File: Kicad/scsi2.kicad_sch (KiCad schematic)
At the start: 29 parts, among them J3 TO-LED, J4 TO-MB, J8 TO-A3000-LED, J9 TO-A3000-MB, U4 NCR53c710 SCSI Host Controller, U7 SST39SF010, Y1 Abracon ACO-50MHz

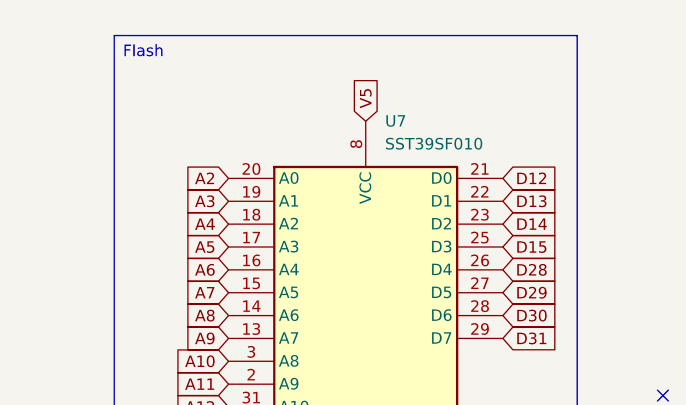
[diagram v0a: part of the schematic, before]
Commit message: Rename all Uxx parts from U1 to U13 for consistency
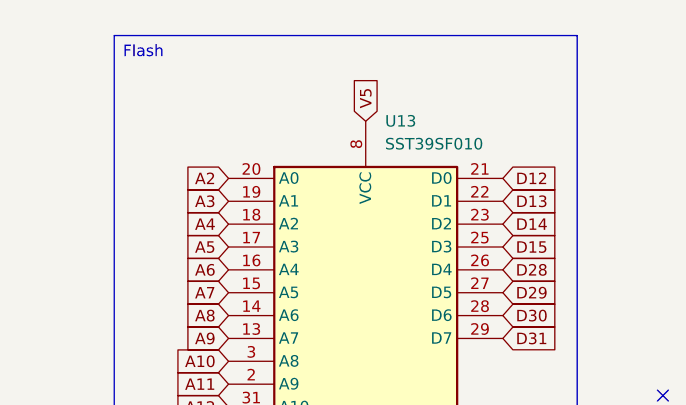
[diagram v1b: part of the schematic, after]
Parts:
- renumbered U4 to U10, U7 to U13
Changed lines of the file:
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@@
 		(dnp no)
 		(fields_autoplaced yes)
-		(property "Reference" "U7"
+		(property "Reference" "U13"
 			(at 259.9533 24.13 0)
 			(effects
@@
 			(project ""
 				(path "/8f9f4021-47aa-41d9-bea7-f6ccf72098bb/2daf4fe3-1e72-4ad5-914a-264df02f69b3"
-					(reference "U7")
+					(reference "U13")
 					(unit 1)
 				)
@@
 		(dnp no)
 		(fields_autoplaced yes)
-		(property "Reference" "U4"
+		(property "Reference" "U10"
 			(at 107.188 12.446 0)
 			(effects
@@
 			(project ""
 				(path "/8f9f4021-47aa-41d9-bea7-f6ccf72098bb/2daf4fe3-1e72-4ad5-914a-264df02f69b3"
-					(reference "U4")
+					(reference "U10")
 					(unit 2)
 				)
@@
 		(dnp no)
 		(fields_autoplaced yes)
-		(property "Reference" "U4"
+		(property "Reference" "U10"
 			(at 32.258 14.986 0)
 			(effects
@@
 			(project ""
 				(path "/8f9f4021-47aa-41d9-bea7-f6ccf72098bb/2daf4fe3-1e72-4ad5-914a-264df02f69b3"
-					(reference "U4")
+					(reference "U10")
 					(unit 1)
 				)

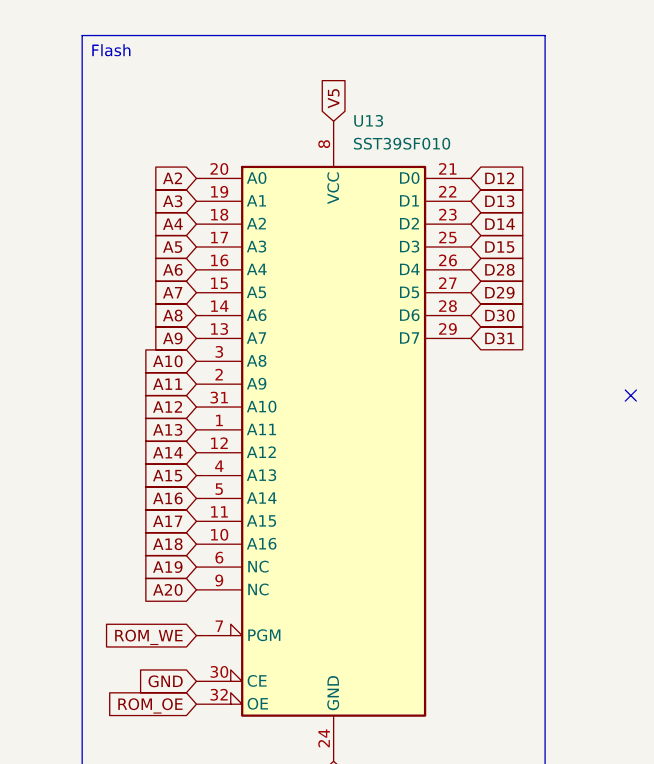
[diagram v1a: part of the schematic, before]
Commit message: Update Flash part symbol
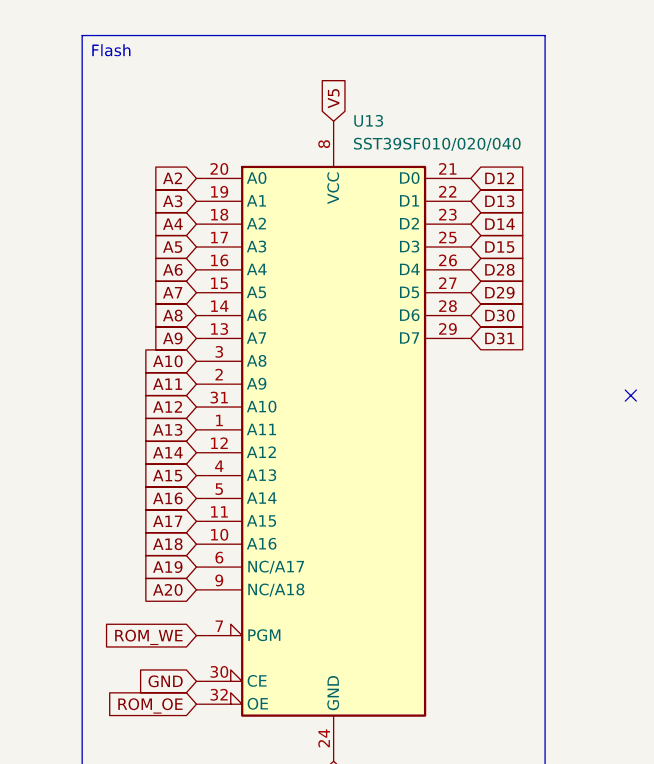
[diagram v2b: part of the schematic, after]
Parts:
- U13: value SST39SF010 -> SST39SF010/020/040
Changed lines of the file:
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@@
 			)
 		)
-		(property "Value" "SST39SF010"
+		(property "Value" "SST39SF010/020/040"
 			(at 259.9533 26.67 0)
 			(effects
@@
 			)
 		)
-		(property "Datasheet" "http://ww1.microchip.com/downloads/en/DeviceDoc/25022B.pdf"
+		(property "Datasheet" "https://ww1.microchip.com/downloads/aemDocuments/documents/MPD/ProductDocuments/DataSheets/SST39SF010A-SST39SF020A-SST39SF040-Data-Sheet-DS20005022.pdf"
 			(at 257.81 53.34 0)
 			(effects

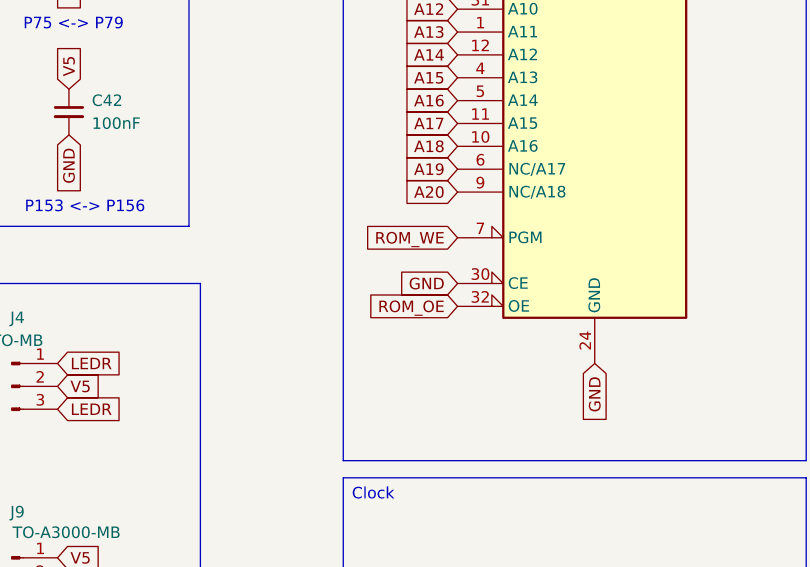
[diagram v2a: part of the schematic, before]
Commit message: ROM_WE Single net Issue #3
Connect ROM_WE to CPLD. Also connect ROM_CE.
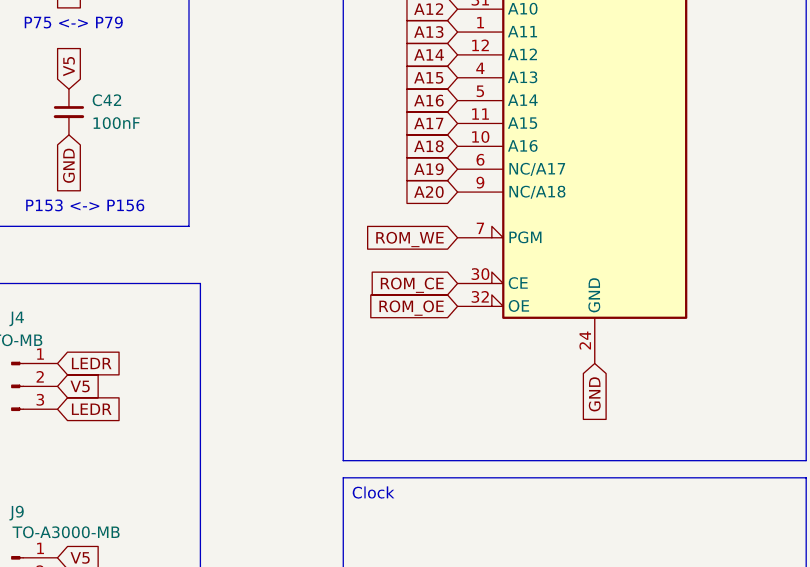
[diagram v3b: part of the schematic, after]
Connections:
- net GND: no longer U13.30 (CE)
- new net ROM_CE: U13.30 (CE)
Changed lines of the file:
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@@
 		)
 	)
-	(global_label "GND"
+	(global_label "ROM_CE"
 		(shape input)
 		(at 242.57 86.36 180)
@@
 		)
 		(property "Intersheetrefs" "${INTERSHEET_REFS}"
-			(at 235.7143 86.36 0)
+			(at 232.1463 86.36 0)
 			(effects
 				(font

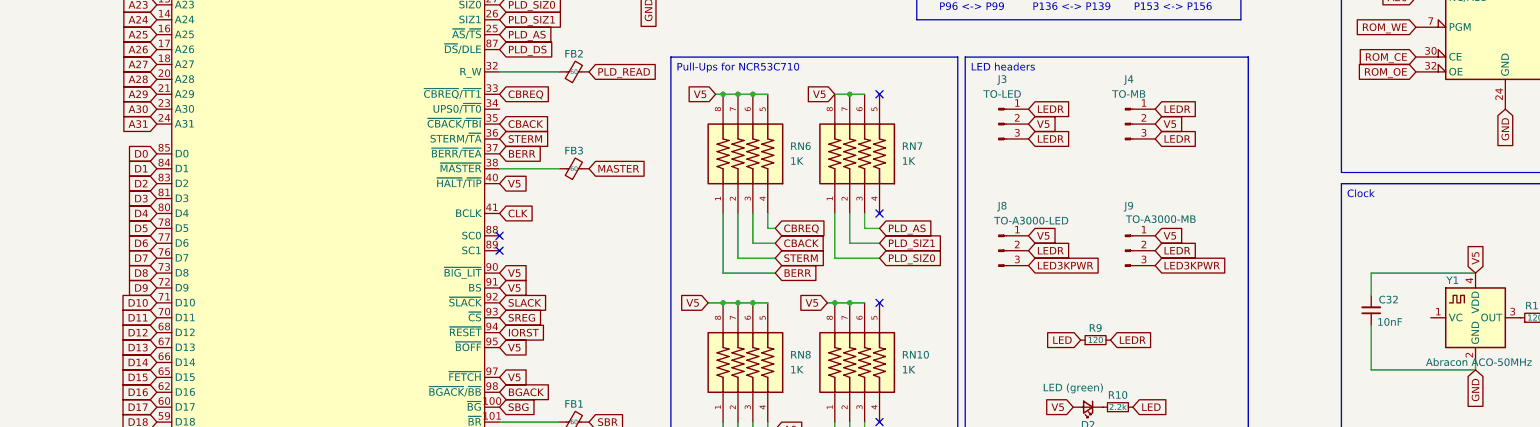
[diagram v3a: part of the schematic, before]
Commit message: Fix various errors from issue #1
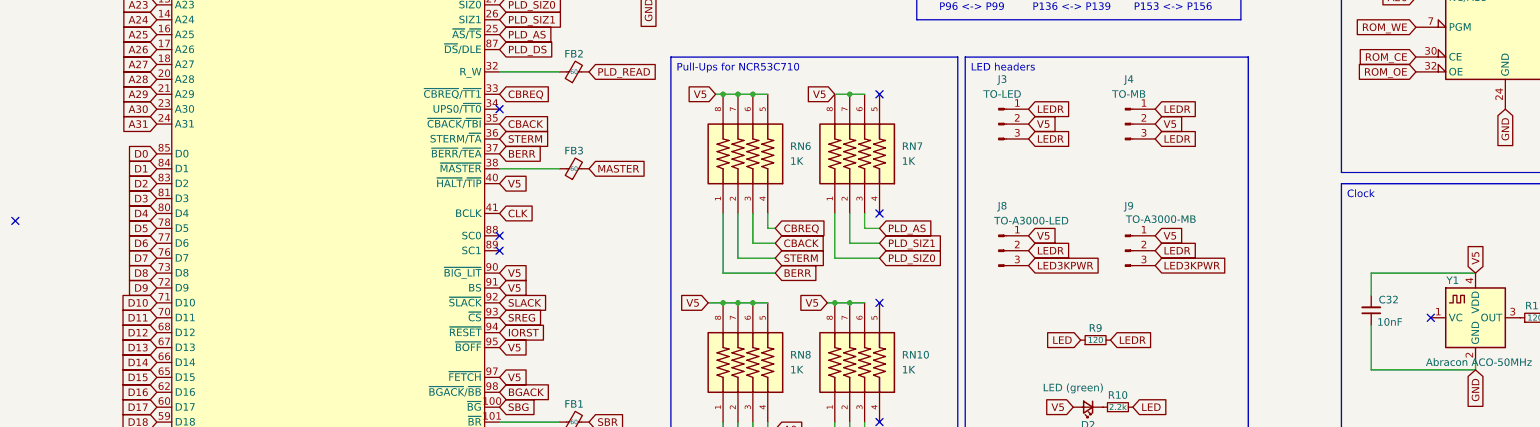
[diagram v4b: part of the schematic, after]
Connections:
- no-connect marks 21 -> 24
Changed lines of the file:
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@@
+	)
+	(no_connect
+		(at 245.11 130.81)
 	)
 	(no_connect
@@
 	)
 	(no_connect
+		(at 86.36 95.25)
+	)
+	(no_connect
 		(at 86.36 34.29)
 	)
 	(no_connect
+		(at 3.81 114.3)
+	)
+	(no_connect

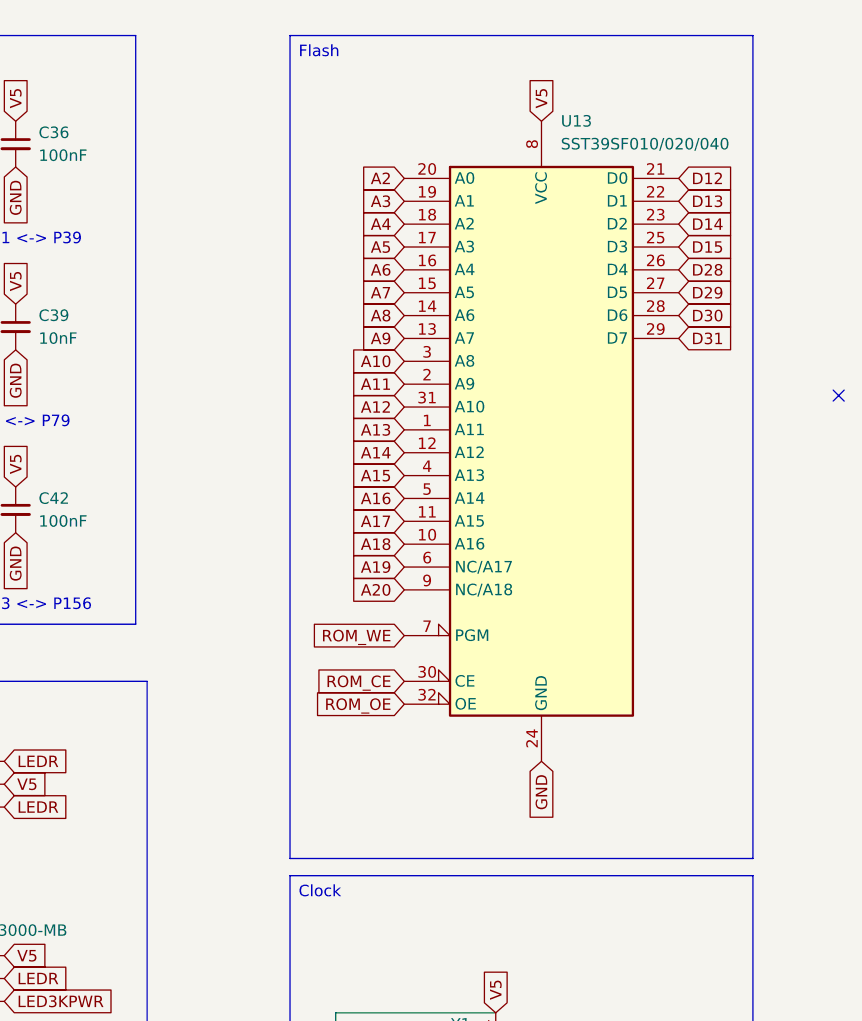
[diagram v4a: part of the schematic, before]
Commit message: Update sheet, add pull down on ROM_CE
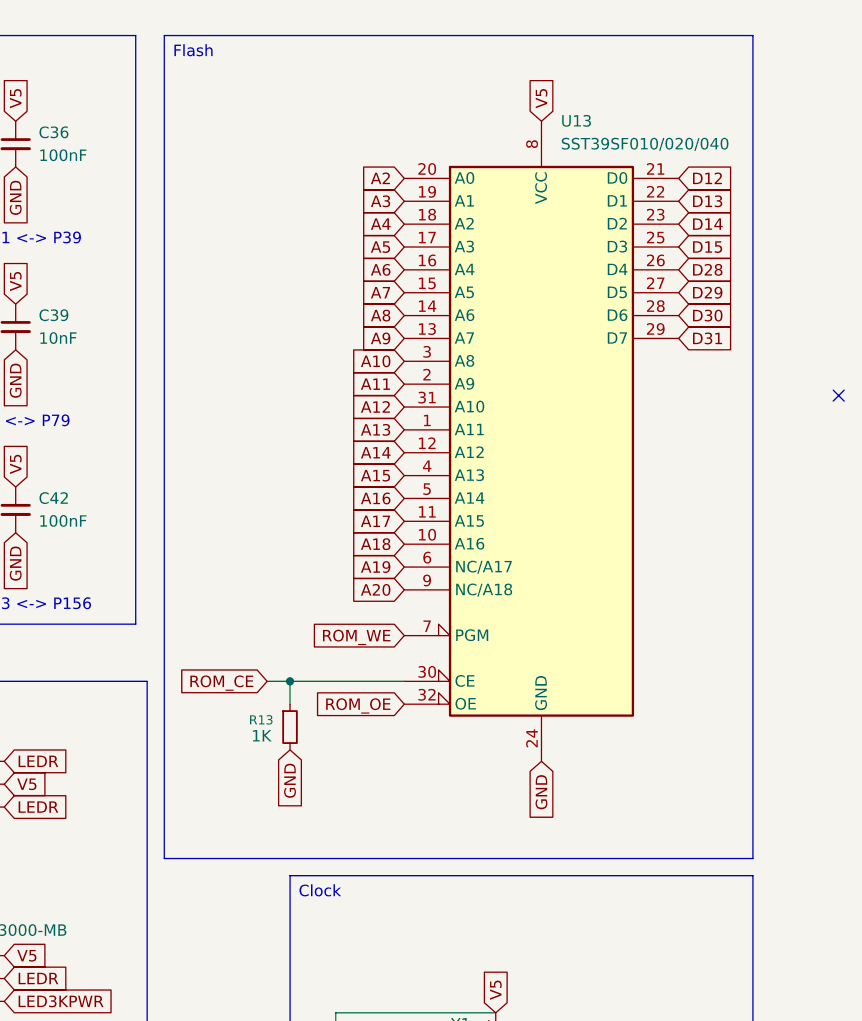
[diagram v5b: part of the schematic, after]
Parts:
- added R13: 1K, symbol Device:R_Small
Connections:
- net GND: now also R13.2
- net ROM_CE: now also R13.1
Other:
- company: (none) -> amiga.technology
- title: (none) -> A4092
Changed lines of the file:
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@@
 	(generator_version "9.0")
 	(paper "A4")
+	(title_block
+		(title "A4092")
+		(rev "PROTO0")
+		(company "amiga.technology")
+	)
 	(text "P2 <-> P6"
 		(exclude_from_sim no)
@@
 	(text_box "Flash\n"
 		(exclude_from_sim no)
-		(at 229.87 14.605 0)
-		(size 51.435 91.44)
+		(at 215.9 14.605 0)
+		(size 65.405 91.44)
 		(margins 0.9525 0.9525 0.9525 0.9525)
 		(stroke
@@
 	)
 	(junction
+		(at 229.87 86.36)
+		(diameter 0)
+		(color 0 0 0 0)
+	)
+	(junction
 		(at 111.76 22.86)
 		(diameter 0)
@@
 	(wire
 		(pts
+			(xy 227.33 86.36) (xy 229.87 86.36)
+		)
+		(stroke
+			(width 0)
+			(type default)
+		)
+	)
+	(wire
+		(pts
 			(xy 111.76 22.86) (xy 115.57 22.86)
 		)
@@
 	(wire
 		(pts
+			(xy 229.87 86.36) (xy 242.57 86.36)
+		)
+		(stroke
+			(width 0)
+			(type default)
+		)
+	)
+	(wire
+		(pts
 			(xy 151.13 38.1) (xy 153.67 38.1)
 		)
@@
 		)
 	)
+	(wire
+		(pts
+			(xy 229.87 88.9) (xy 229.87 86.36)
+		)
+		(stroke
+			(width 0)
+			(type default)
+		)
+	)
 	(global_label "SCDAT0"
 		(shape input)
@@
 	(global_label "ROM_CE"
 		(shape input)
-		(at 242.57 86.36 180)
+		(at 227.33 86.36 180)
 		(fields_autoplaced yes)
 		(effects
@@
 		)
 		(property "Intersheetrefs" "${INTERSHEET_REFS}"
-			(at 232.1463 86.36 0)
+			(at 216.9063 86.36 0)
 			(effects
 				(font
@@
 		)
 	)
+	(global_label "GND"
+		(shape input)
+		(at 229.87 93.98 270)
+		(fields_autoplaced yes)
+		(effects
+			(font
+				(size 1.27 1.27)
+			)
+			(justify right)
+		)
+		(property "Intersheetrefs" "${INTERSHEET_REFS}"
+			(at 229.87 100.8357 90)
+			(effects
+				(font
+					(size 1.27 1.27)
+				)
+				(justify right)
+				(hide yes)
+			)
+		)
+	)
 	(global_label "V5"
 		(shape input)
@@
 					(unit 1)
 				)
+			)
+		)
+	)
+	(symbol
+		(lib_name "R_Small_1")
+		(lib_id "Device:R_Small")
+		(at 229.87 91.44 0)
+		(unit 1)
+		(exclude_from_sim no)
+		(in_bom yes)
+		(on_board yes)
+		(dnp no)
+		(property "Reference" "R13"
+			(at 225.298 90.678 0)
+			(effects
+				(font
+					(size 1.016 1.016)
+				)
+				(justify left)
+			)
+		)
+		(property "Value" "1K"
+			(at 225.552 92.456 0)
+			(effects
+				(font
+					(size 1.27 1.27)
+				)
+				(justify left)
+			)
+		)
+		(property "Footprint" ""
+			(at 229.87 91.44 0)
+			(effects
+				(font
+					(size 1.27 1.27)
+				)
+				(hide yes)
+			)
+		)
+		(property "Datasheet" "~"
+			(at 229.87 91.44 0)
+			(effects
+				(font
+					(size 1.27 1.27)
+				)
+				(hide yes)
+			)
+		)
+		(property "Description" "Resistor, small symbol"
+			(at 229.87 91.44 0)
+			(effects
+				(font
+					(size 1.27 1.27)
+				)
+				(hide yes)
+			)
+		)
+		(pin "2"
+		)
+		(pin "1"
+		)
+		(instances
+			(project ""
+				(path "/8f9f4021-47aa-41d9-bea7-f6ccf72098bb/2daf4fe3-1e72-4ad5-914a-264df02f69b3"
+					(reference "R13")
+					(unit 1)
+				)

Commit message: Add footprint to pull down of ROM_CE
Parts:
- R13: footprint (none) -> Resistor_SMD:R_0603_1608Metric
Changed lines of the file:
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@@
 			)
 		)
-		(property "Footprint" ""
+		(property "Footprint" "Resistor_SMD:R_0603_1608Metric"
 			(at 229.87 91.44 0)
 			(effects

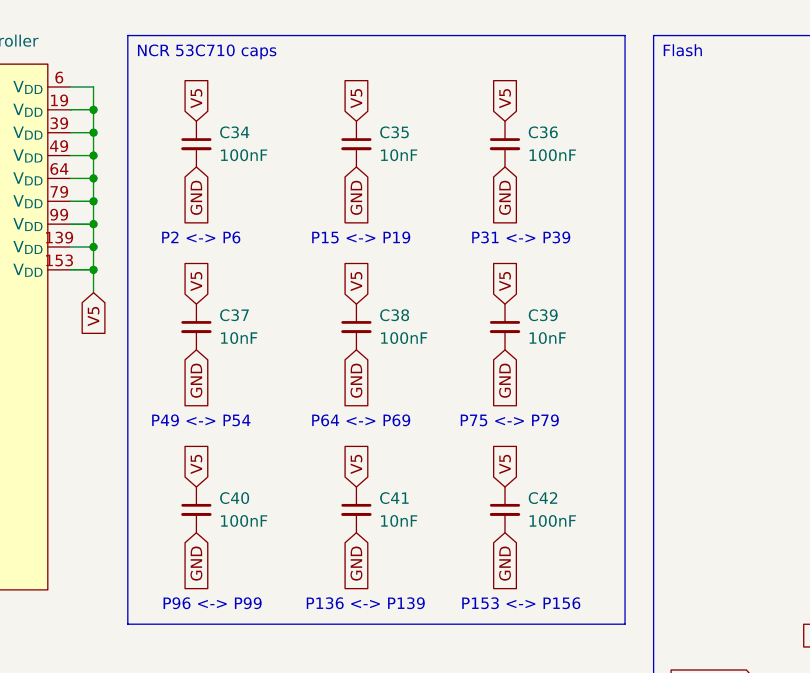
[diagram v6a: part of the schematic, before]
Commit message: Rename capacitors
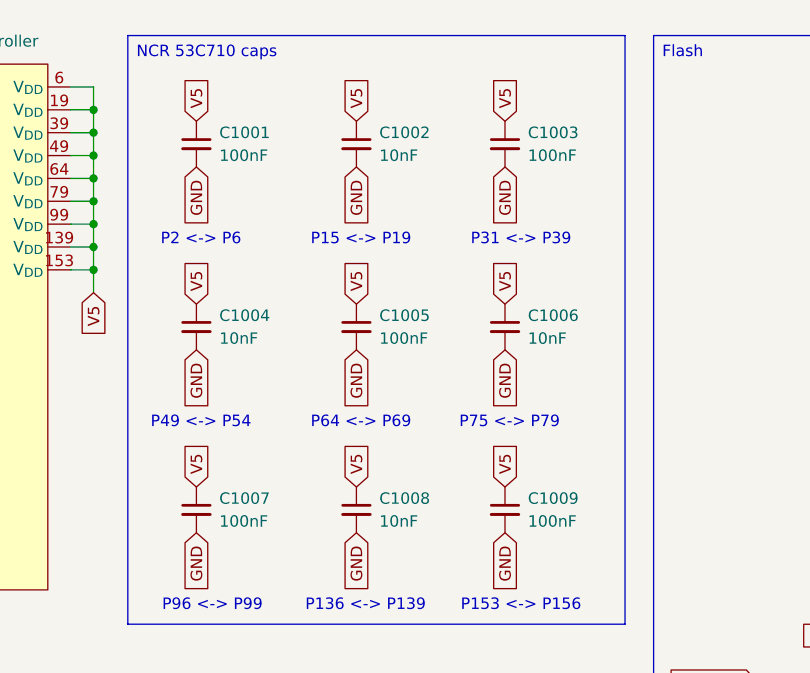
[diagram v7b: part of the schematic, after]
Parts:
- renumbered C34 to C1001, C35 to C1002, C36 to C1003, C37 to C1004, C38 to C1005, C39 to C1006, C40 to C1007, C41 to C1008, C42 to C1009
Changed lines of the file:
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@@
 		(dnp no)
 		(fields_autoplaced yes)
-		(property "Reference" "C42"
+		(property "Reference" "C1009"
 			(at 201.93 66.0462 0)
 			(effects
@@
 			(project "A4092"
 				(path "/8f9f4021-47aa-41d9-bea7-f6ccf72098bb/2daf4fe3-1e72-4ad5-914a-264df02f69b3"
-					(reference "C42")
+					(reference "C1009")
 					(unit 1)
 				)
@@
 		(dnp no)
 		(fields_autoplaced yes)
-		(property "Reference" "C34"
+		(property "Reference" "C1001"
 			(at 167.64 25.4062 0)
 			(effects
@@
 			(project "A4092"
 				(path "/8f9f4021-47aa-41d9-bea7-f6ccf72098bb/2daf4fe3-1e72-4ad5-914a-264df02f69b3"
-					(reference "C34")
+					(reference "C1001")
 					(unit 1)
 				)
@@
 		(dnp no)
 		(fields_autoplaced yes)
-		(property "Reference" "C37"
+		(property "Reference" "C1004"
 			(at 167.64 45.7262 0)
 			(effects
@@
 			(project "A4092"
 				(path "/8f9f4021-47aa-41d9-bea7-f6ccf72098bb/2daf4fe3-1e72-4ad5-914a-264df02f69b3"
-					(reference "C37")
+					(reference "C1004")
 					(unit 1)
 				)
@@
 		(dnp no)
 		(fields_autoplaced yes)
-		(property "Reference" "C38"
+		(property "Reference" "C1005"
 			(at 185.42 45.7262 0)
 			(effects
@@
 			(project "A4092"
 				(path "/8f9f4021-47aa-41d9-bea7-f6ccf72098bb/2daf4fe3-1e72-4ad5-914a-264df02f69b3"
-					(reference "C38")
+					(reference "C1005")
 					(unit 1)
 				)
@@
 		(dnp no)
 		(fields_autoplaced yes)
-		(property "Reference" "C40"
+		(property "Reference" "C1007"
 			(at 167.64 66.0462 0)
 			(effects
@@
 			(project "A4092"
 				(path "/8f9f4021-47aa-41d9-bea7-f6ccf72098bb/2daf4fe3-1e72-4ad5-914a-264df02f69b3"
-					(reference "C40")
+					(reference "C1007")
 					(unit 1)
 				)
@@
 		(dnp no)
 		(fields_autoplaced yes)
-		(property "Reference" "C41"
+		(property "Reference" "C1008"
 			(at 185.42 66.0462 0)
 			(effects
@@
 			(project "A4092"
 				(path "/8f9f4021-47aa-41d9-bea7-f6ccf72098bb/2daf4fe3-1e72-4ad5-914a-264df02f69b3"
-					(reference "C41")
+					(reference "C1008")
 					(unit 1)
 				)
@@
 		(dnp no)
 		(fields_autoplaced yes)
-		(property "Reference" "C39"
+		(property "Reference" "C1006"
 			(at 201.93 45.7262 0)
 			(effects
@@
 			(project "A4092"
 				(path "/8f9f4021-47aa-41d9-bea7-f6ccf72098bb/2daf4fe3-1e72-4ad5-914a-264df02f69b3"
-					(reference "C39")
+					(reference "C1006")
 					(unit 1)
 				)
@@
 		(dnp no)
 		(fields_autoplaced yes)
-		(property "Reference" "C36"
+		(property "Reference" "C1003"
 			(at 201.93 25.4062 0)
 			(effects
@@
 			(project "A4092"
 				(path "/8f9f4021-47aa-41d9-bea7-f6ccf72098bb/2daf4fe3-1e72-4ad5-914a-264df02f69b3"
-					(reference "C36")
+					(reference "C1003")
 					(unit 1)
 				)
@@
 		(dnp no)
 		(fields_autoplaced yes)
-		(property "Reference" "C35"
+		(property "Reference" "C1002"
 			(at 185.42 25.4062 0)
 			(effects
@@
 			(project "A4092"
 				(path "/8f9f4021-47aa-41d9-bea7-f6ccf72098bb/2daf4fe3-1e72-4ad5-914a-264df02f69b3"
-					(reference "C35")
-					(unit 1)
-				)
+					(reference "C1002")
+					(unit 1)
+				)
